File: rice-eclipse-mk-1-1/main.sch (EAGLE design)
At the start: 56 parts, among them U1 LM1084ISX-5.0/NOPB, U2 THS4531IDRD8-M, U3 THS4531IDRD8-M, U4 THS4531IDRD8-M, U5 THS4531IDRD8-M, X1 2540-5

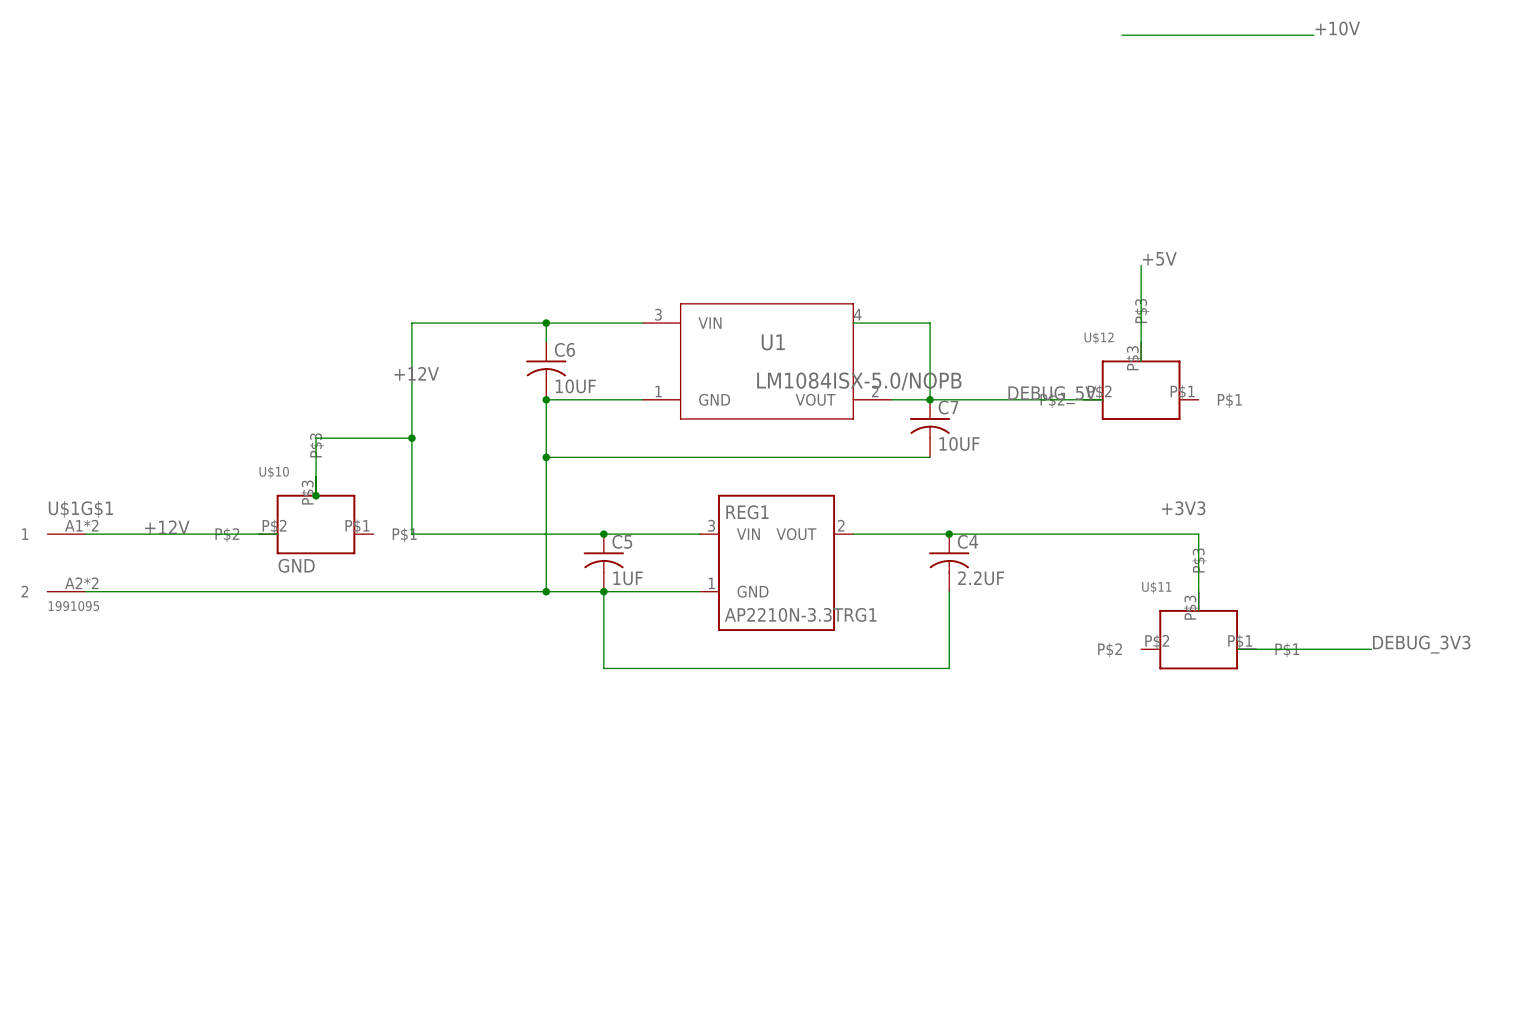
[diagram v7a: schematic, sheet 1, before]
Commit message: Added new libraries and fixed board annotation.
LEDS had to be removed in the process. Will re-add in next
version. I'm mostly just happy that the board is fixed.
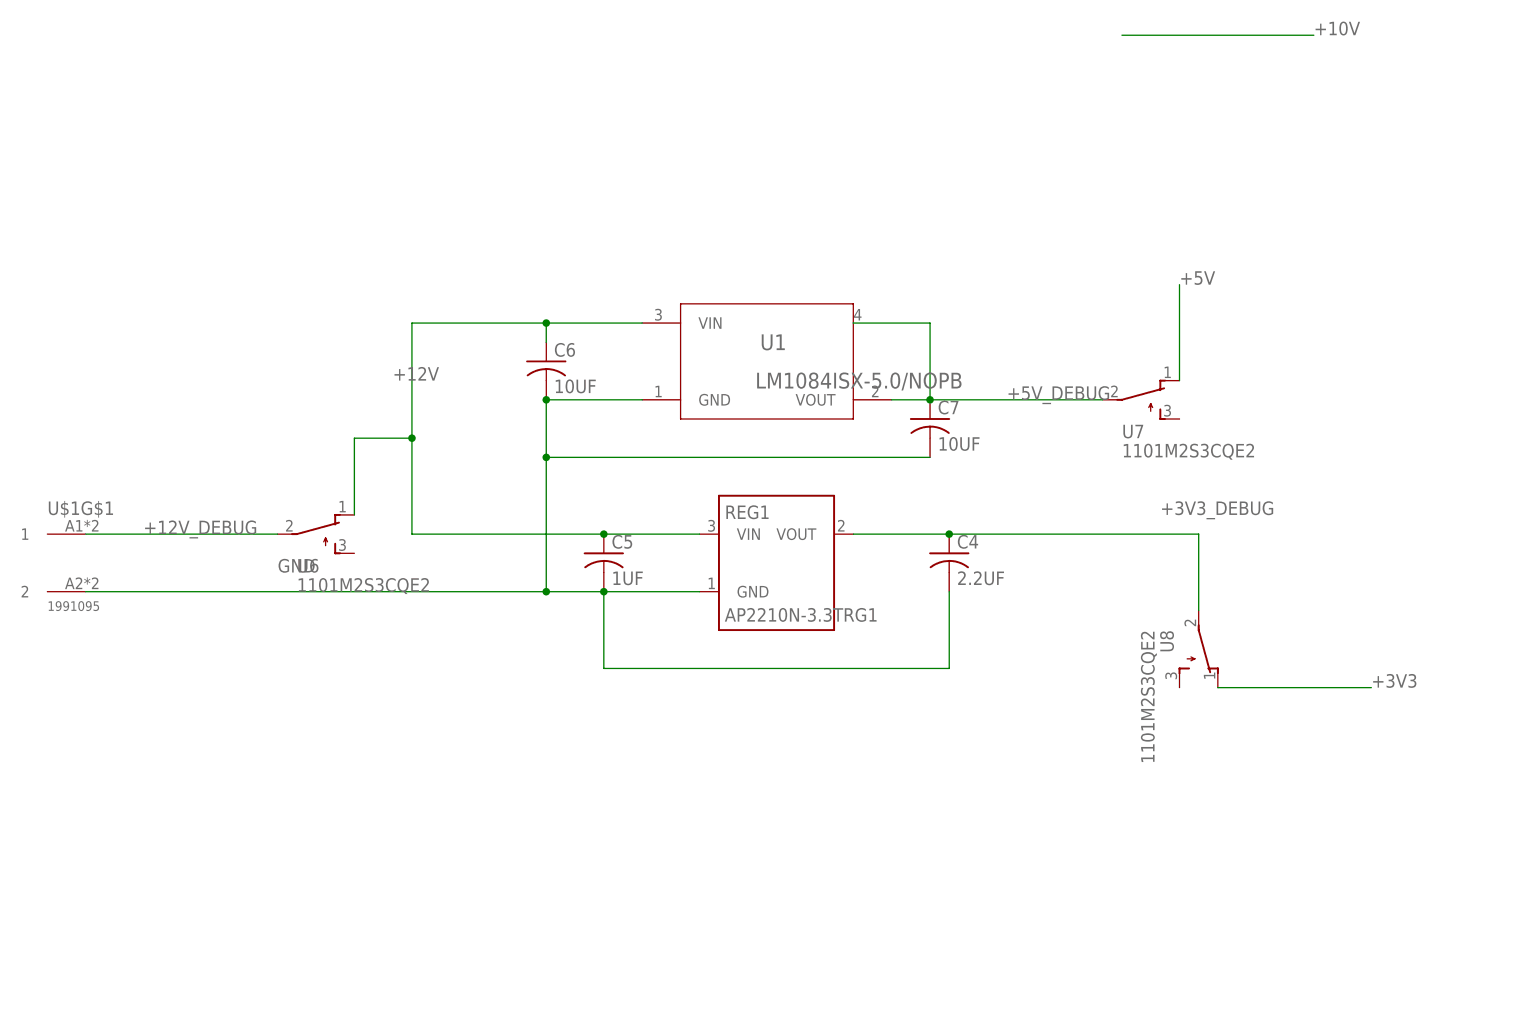
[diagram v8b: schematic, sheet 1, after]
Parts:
- removed U$10, U$11, U$12: SLIDE_SW, SLIDE_SW:SLIDE_SW
- added U6, U7, U8: 1101M2S3CQE2, SLIDE_SW:1101M2S3CQE2
- C10, C11, C12, C13, C3: device resistor:C-USC0603 -> rcl:C-USC0603
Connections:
- removed net DEBUG_3V3: U$11.P$1
- removed net DEBUG_5V: C7.1, U$12.P$2, U1.4, U1.VOUT
- new net +12V_DEBUG: U$1G$1.1, U6.P
- new net +3V3_DEBUG: C4.1, REG1.VOUT, U8.P
- new net +5V_DEBUG: C7.1, U1.4, U1.VOUT, U7.P
- net +12V: now also U6.O; no longer U$10.P$2, U$10.P$3, U$1G$1.1
- net +3V3: no longer C4.1, REG1.VOUT, U$11.P$3
- net +5V: no longer U$12.P$3
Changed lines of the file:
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@@
 <part name="FRAME3" library="frames" library_urn="urn:adsk.eagle:library:229" deviceset="A4L-LOC" device=""/>
 <part name="ADC1" library="microchip-extra" deviceset="MCP3208" device="SN"/>
-<part name="C3" library="resistor" library_urn="urn:adsk.eagle:library:348" deviceset="C-US" device="C0603" package3d_urn="urn:adsk.eagle:package:26138/1" value="1UF"/>
+<part name="C3" library="rcl" library_urn="urn:adsk.eagle:library:334" deviceset="C-US" device="C0603" package3d_urn="urn:adsk.eagle:package:23616/2" value="1UF"/>
 <part name="REG1" library="diodes-extra" deviceset="AP2210N-3.3TRG1" device=""/>
 <part name="C4" library="rcl" library_urn="urn:adsk.eagle:library:334" deviceset="C-US" device="C0603" package3d_urn="urn:adsk.eagle:package:23616/2" value="2.2UF"/>
@@
 <part name="R11" library="rcl" library_urn="urn:adsk.eagle:library:334" deviceset="R-US_" device="R0603" package3d_urn="urn:adsk.eagle:package:23555/2" value="20K"/>
 <part name="R14" library="rcl" library_urn="urn:adsk.eagle:library:334" deviceset="R-US_" device="R0603" package3d_urn="urn:adsk.eagle:package:23555/2" value="20K"/>
-<part name="C10" library="resistor" library_urn="urn:adsk.eagle:library:348" deviceset="C-US" device="C0603" package3d_urn="urn:adsk.eagle:package:26138/1" value="1UF"/>
+<part name="C10" library="rcl" library_urn="urn:adsk.eagle:library:334" deviceset="C-US" device="C0603" package3d_urn="urn:adsk.eagle:package:23616/2" value="1UF"/>
 <part name="U3" library="texas-extra" deviceset="THS4531IDR" device="D8-M"/>
 <part name="R12" library="rcl" library_urn="urn:adsk.eagle:library:334" deviceset="R-US_" device="R0603" package3d_urn="urn:adsk.eagle:package:23555/2" value="33K"/>
@@
 <part name="R15" library="rcl" library_urn="urn:adsk.eagle:library:334" deviceset="R-US_" device="R0603" package3d_urn="urn:adsk.eagle:package:23555/2" value="20K"/>
 <part name="R16" library="rcl" library_urn="urn:adsk.eagle:library:334" deviceset="R-US_" device="R0603" package3d_urn="urn:adsk.eagle:package:23555/2" value="20K"/>
-<part name="C11" library="resistor" library_urn="urn:adsk.eagle:library:348" deviceset="C-US" device="C0603" package3d_urn="urn:adsk.eagle:package:26138/1" value="1UF"/>
+<part name="C11" library="rcl" library_urn="urn:adsk.eagle:library:334" deviceset="C-US" device="C0603" package3d_urn="urn:adsk.eagle:package:23616/2" value="1UF"/>
 <part name="U4" library="texas-extra" deviceset="THS4531IDR" device="D8-M"/>
 <part name="R17" library="rcl" library_urn="urn:adsk.eagle:library:334" deviceset="R-US_" device="R0603" package3d_urn="urn:adsk.eagle:package:23555/2" value="33K"/>
@@
 <part name="R19" library="rcl" library_urn="urn:adsk.eagle:library:334" deviceset="R-US_" device="R0603" package3d_urn="urn:adsk.eagle:package:23555/2" value="20K"/>
 <part name="R20" library="rcl" library_urn="urn:adsk.eagle:library:334" deviceset="R-US_" device="R0603" package3d_urn="urn:adsk.eagle:package:23555/2" value="20K"/>
-<part name="C12" library="resistor" library_urn="urn:adsk.eagle:library:348" deviceset="C-US" device="C0603" package3d_urn="urn:adsk.eagle:package:26138/1" value="1UF"/>
+<part name="C12" library="rcl" library_urn="urn:adsk.eagle:library:334" deviceset="C-US" device="C0603" package3d_urn="urn:adsk.eagle:package:23616/2" value="1UF"/>
 <part name="U5" library="texas-extra" deviceset="THS4531IDR" device="D8-M"/>
 <part name="R21" library="rcl" library_urn="urn:adsk.eagle:library:334" deviceset="R-US_" device="R0603" package3d_urn="urn:adsk.eagle:package:23555/2" value="33K"/>
@@
 <part name="R23" library="rcl" library_urn="urn:adsk.eagle:library:334" deviceset="R-US_" device="R0603" package3d_urn="urn:adsk.eagle:package:23555/2" value="20K"/>
 <part name="R24" library="rcl" library_urn="urn:adsk.eagle:library:334" deviceset="R-US_" device="R0603" package3d_urn="urn:adsk.eagle:package:23555/2" value="20K"/>
-<part name="C13" library="resistor" library_urn="urn:adsk.eagle:library:348" deviceset="C-US" device="C0603" package3d_urn="urn:adsk.eagle:package:26138/1" value="1UF"/>
+<part name="C13" library="rcl" library_urn="urn:adsk.eagle:library:334" deviceset="C-US" device="C0603" package3d_urn="urn:adsk.eagle:package:23616/2" value="1UF"/>
 <part name="R25" library="rcl" library_urn="urn:adsk.eagle:library:334" deviceset="R-US_" device="R0603" package3d_urn="urn:adsk.eagle:package:23555/2" value="500K"/>
 <part name="X5" library="con-phoenix-250-extra" deviceset="1770908" device=""/>
 <part name="X6" library="con-phoenix-250-extra" deviceset="1770908" device=""/>
-<part name="U$10" library="SLIDE_SW" deviceset="SLIDE_SW" device=""/>
-<part name="U$11" library="SLIDE_SW" deviceset="SLIDE_SW" device=""/>
-<part name="U$12" library="SLIDE_SW" deviceset="SLIDE_SW" device=""/>
+<part name="U6" library="SLIDE_SW" deviceset="1101M2S3CQE2" device=""/>
+<part name="U7" library="SLIDE_SW" deviceset="1101M2S3CQE2" device=""/>
+<part name="U8" library="SLIDE_SW" deviceset="1101M2S3CQE2" device=""/>
 </parts>
 <sheets>
@@
 <instance part="U$1" gate="G$1" x="58.42" y="93.98"/>
 <instance part="U$1" gate="G$2" x="58.42" y="86.36"/>
-<instance part="U$10" gate="G$1" x="88.9" y="93.98"/>
-<instance part="U$11" gate="G$1" x="205.74" y="78.74"/>
-<instance part="U$12" gate="G$1" x="198.12" y="111.76"/>
+<instance part="U6" gate="A" x="88.9" y="93.98" rot="R270"/>
+<instance part="U7" gate="A" x="198.12" y="111.76" rot="R270"/>
+<instance part="U8" gate="A" x="205.74" y="78.74" rot="R180"/>
 </instances>
 <busses>
@@
 <junction x="127" y="93.98"/>
 <wire x1="101.6" y1="93.98" x2="127" y2="93.98" width="0.1524" layer="91"/>
-<pinref part="U$10" gate="G$1" pin="P$3"/>
-<wire x1="88.9" y1="99.06" x2="88.9" y2="101.6" width="0.1524" layer="91"/>
-<wire x1="88.9" y1="99.06" x2="88.9" y2="106.68" width="0.1524" layer="91"/>
-<junction x="88.9" y="99.06"/>
 <pinref part="C6" gate="G$1" pin="1"/>
 <wire x1="119.38" y1="121.92" x2="119.38" y2="119.38" width="0.1524" layer="91"/>
@@
 <wire x1="132.08" y1="121.92" x2="119.38" y2="121.92" width="0.1524" layer="91"/>
 <label x="99.06" y="114.3" size="1.778" layer="95"/>
-<wire x1="88.9" y1="106.68" x2="101.6" y2="106.68" width="0.1524" layer="91"/>
+<wire x1="93.98" y1="106.68" x2="101.6" y2="106.68" width="0.1524" layer="91"/>
 <wire x1="101.6" y1="106.68" x2="101.6" y2="121.92" width="0.1524" layer="91"/>
 <wire x1="101.6" y1="93.98" x2="101.6" y2="106.68" width="0.1524" layer="91"/>
 <junction x="101.6" y="106.68"/>
-</segment>
-<segment>
-<pinref part="U$10" gate="G$1" pin="P$2"/>
-<pinref part="U$1" gate="G$1" pin="1"/>
-<wire x1="83.82" y1="93.98" x2="58.42" y2="93.98" width="0.1524" layer="91"/>
-<label x="66.04" y="93.98" size="1.778" layer="95"/>
+<pinref part="U6" gate="A" pin="O"/>
+<wire x1="93.98" y1="96.52" x2="93.98" y2="106.68" width="0.1524" layer="91"/>
 </segment>
 </net>
 <net name="+3V3" class="0">
 <segment>
-<wire x1="160.02" y1="93.98" x2="172.72" y2="93.98" width="0.1524" layer="91"/>
-<label x="200.66" y="96.52" size="1.778" layer="95"/>
-<pinref part="REG1" gate="G$1" pin="VOUT"/>
-<pinref part="C4" gate="G$1" pin="1"/>
-<wire x1="172.72" y1="93.98" x2="205.74" y2="93.98" width="0.1524" layer="91"/>
-<junction x="172.72" y="93.98"/>
-<pinref part="U$11" gate="G$1" pin="P$3"/>
-<wire x1="205.74" y1="93.98" x2="205.74" y2="83.82" width="0.1524" layer="91"/>
+<wire x1="208.28" y1="73.66" x2="228.6" y2="73.66" width="0.1524" layer="91"/>
+<label x="228.6" y="73.66" size="1.778" layer="95"/>
 </segment>
 </net>
 <net name="+5V" class="0">
 <segment>
-<pinref part="U$12" gate="G$1" pin="P$3"/>
-<wire x1="198.12" y1="116.84" x2="198.12" y2="129.54" width="0.1524" layer="91"/>
-<label x="198.12" y="129.54" size="1.778" layer="95"/>
+<wire x1="203.2" y1="114.3" x2="203.2" y2="127" width="0.1524" layer="91"/>
+<label x="203.2" y="127" size="1.778" layer="95"/>
 </segment>
 </net>
@@
 </segment>
 </net>
-<net name="DEBUG_3V3" class="0">
+<net name="+12V_DEBUG" class="0">
 <segment>
-<pinref part="U$11" gate="G$1" pin="P$1"/>
-<wire x1="210.82" y1="78.74" x2="228.6" y2="78.74" width="0.1524" layer="91"/>
-<label x="228.6" y="78.74" size="1.778" layer="95"/>
+<pinref part="U$1" gate="G$1" pin="1"/>
+<wire x1="83.82" y1="93.98" x2="58.42" y2="93.98" width="0.1524" layer="91"/>
+<label x="66.04" y="93.98" size="1.778" layer="95"/>
+<pinref part="U6" gate="A" pin="P"/>
 </segment>
 </net>
-<net name="DEBUG_5V" class="0">
+<net name="+5V_DEBUG" class="0">
 <segment>
 <label x="180.34" y="111.76" size="1.778" layer="95"/>
@@
 <wire x1="160.02" y1="121.92" x2="170.18" y2="121.92" width="0.1524" layer="91"/>
 <wire x1="170.18" y1="121.92" x2="170.18" y2="111.76" width="0.1524" layer="91"/>
-<pinref part="U$12" gate="G$1" pin="P$2"/>
+<pinref part="U7" gate="A" pin="P"/>
 </segment>
 </net>
+<net name="+3V3_DEBUG" class="0">
+<segment>
+<wire x1="160.02" y1="93.98" x2="172.72" y2="93.98" width="0.1524" layer="91"/>
+<label x="200.66" y="96.52" size="1.778" layer="95"/>
+<pinref part="REG1" gate="G$1" pin="VOUT"/>
+<pinref part="C4" gate="G$1" pin="1"/>
+<wire x1="172.72" y1="93.98" x2="205.74" y2="93.98" width="0.1524" layer="91"/>
+<junction x="172.72" y="93.98"/>
+<wire x1="205.74" y1="93.98" x2="205.74" y2="83.82" width="0.1524" layer="91"/>
+<pinref part="U8" gate="A" pin="P"/>
+</segment>
+</net>
